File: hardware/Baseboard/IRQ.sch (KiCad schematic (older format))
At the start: 4 parts, among them IC11 74HC148, IC12 74HC273

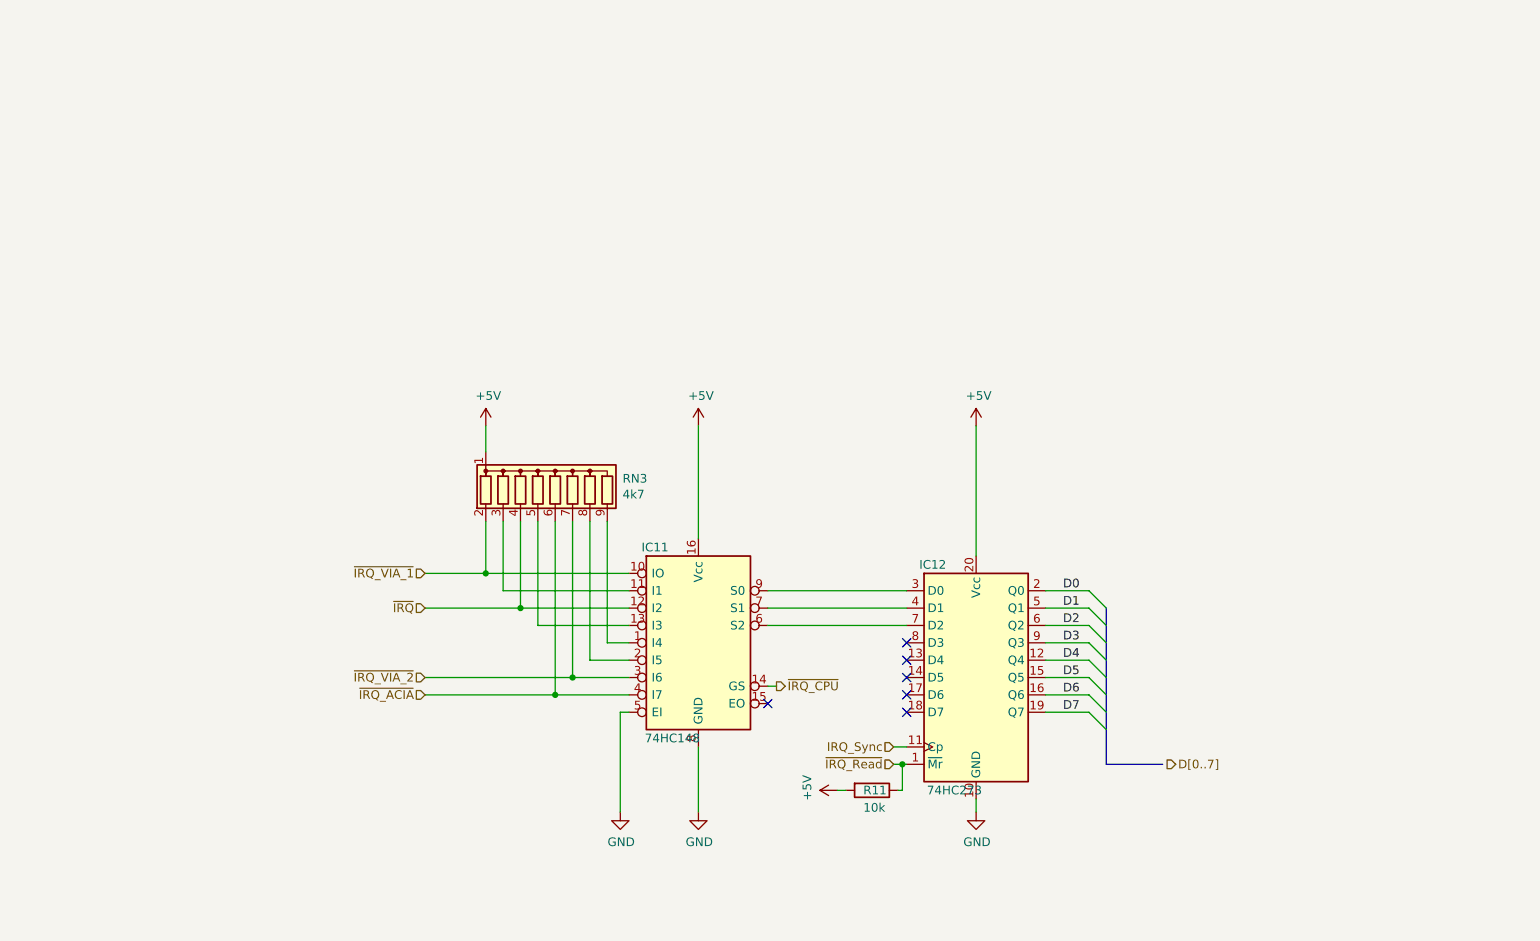
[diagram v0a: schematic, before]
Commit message: Improve routing, add some datasheet recommendations
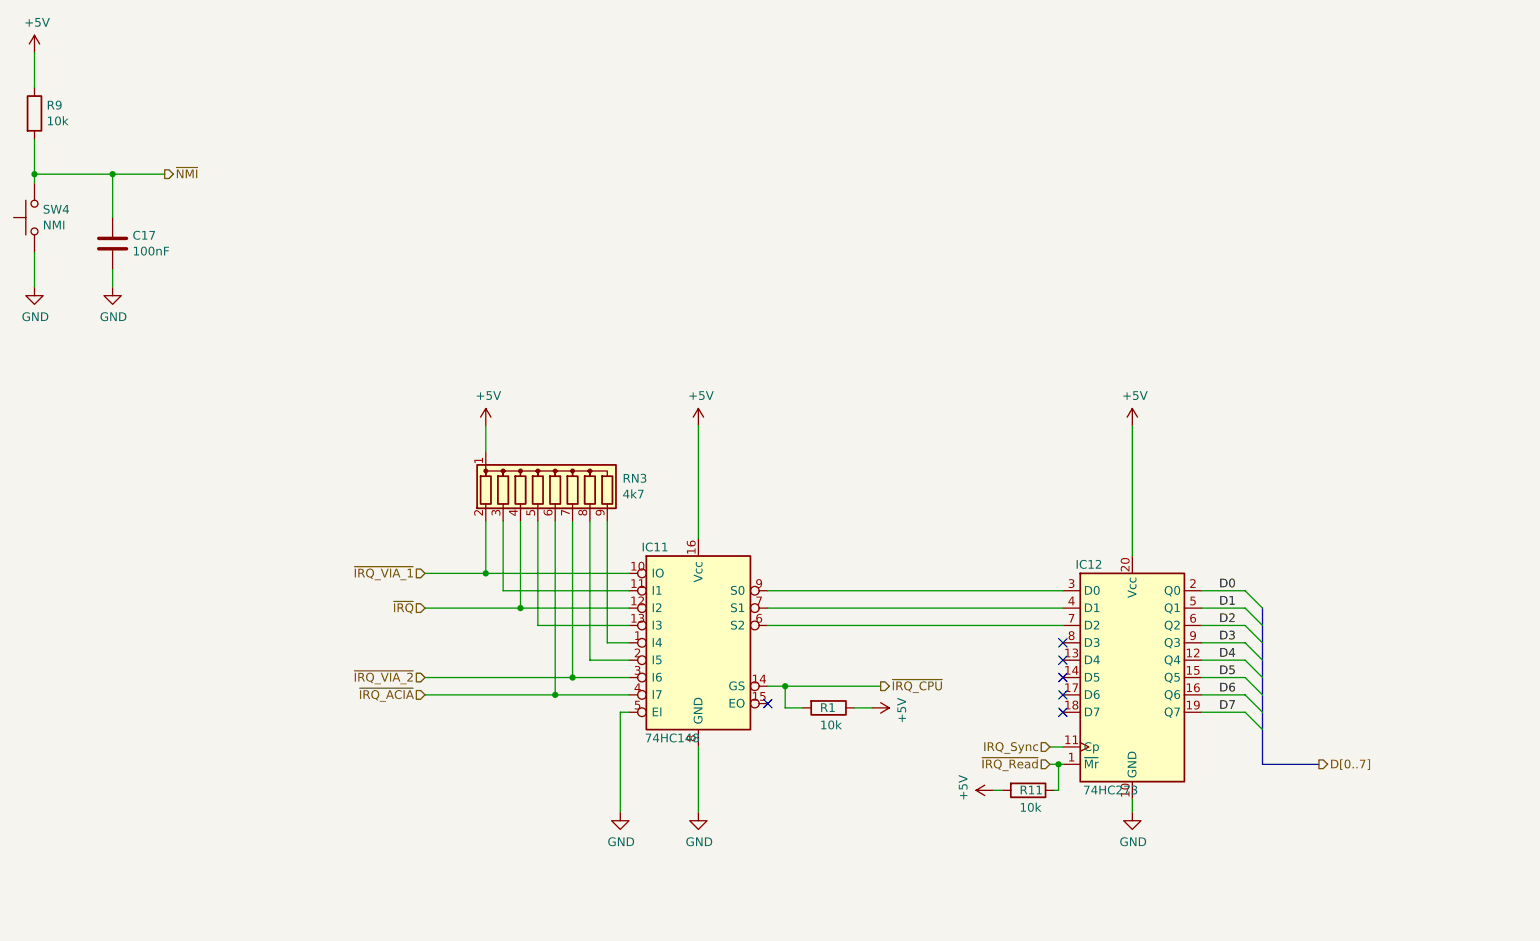
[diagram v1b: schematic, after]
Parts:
- added C17: 100nF, Capacitor_THT:C_Rect_L4.0mm_W2.5mm_P2.50mm, symbol Device:C
- added R1, R9: 10k, Resistor_THT:R_Axial_DIN0207_L6.3mm_D2.5mm_P7.62mm_Horizontal, symbol Device:R
- added SW4: NMI, Button_Switch_THT:SW_PUSH_6mm_H4.3mm, symbol Switch:SW_Push
- IC11: footprint Package_DIP:DIP-16_W7.62mm -> Package_DIP:DIP-16_W7.62mm_LongPads
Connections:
- net +5V: now also R1.1, R9.1
- net GND: now also C17.2, SW4.1
- net ~IRQ_CPU: now also R1.2
- new net ~NMI: C17.1, R9.2, SW4.2
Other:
- moved on the sheet: IC12, R11

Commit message: Optimize routing
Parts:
- IC12: footprint Package_DIP:DIP-20_W7.62mm -> Package_DIP:DIP-20_W7.62mm_LongPads
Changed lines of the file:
@@
 F 0 "IC12" H 6950 5175 50  0000 C CNN
 F 1 "74HC273" H 7075 3875 50  0000 C CNN
-F 2 "Package_DIP:DIP-20_W7.62mm" H 7200 4525 50  0001 C CNN
+F 2 "Package_DIP:DIP-20_W7.62mm_LongPads" H 7200 4525 50  0001 C CNN
 F 3 "https://assets.nexperia.com/documents/data-sheet/74HC_HCT273.pdf" H 7200 4525 50  0001 C CNN
 F 4 "Texas Instruments" H 7200 4525 50  0001 C CNN "Mfr."

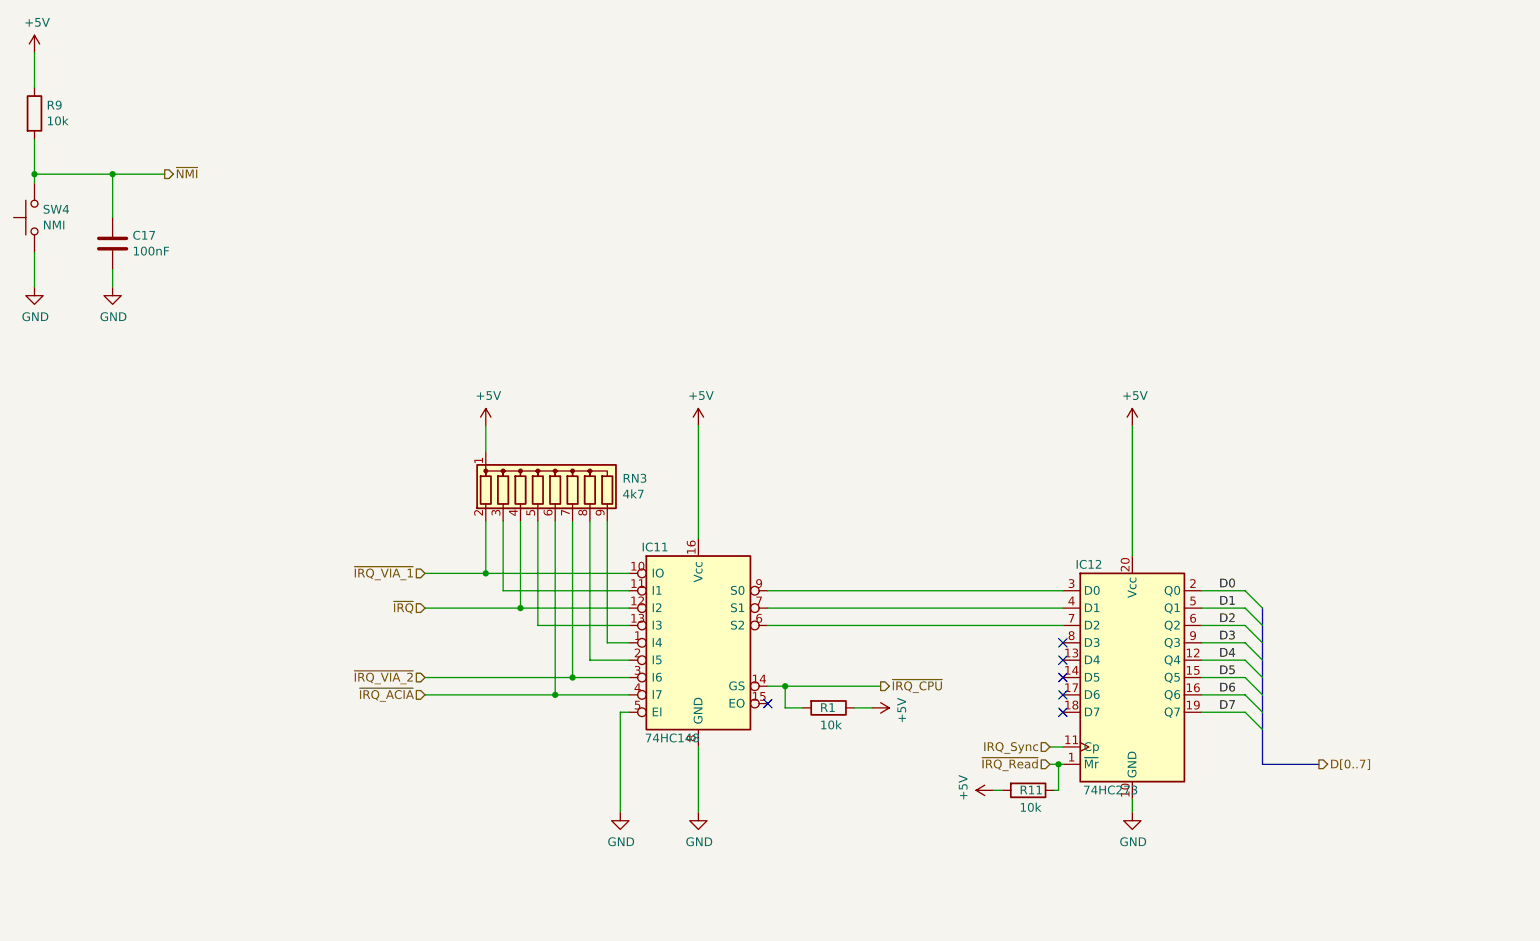
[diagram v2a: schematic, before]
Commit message: Optimize routing, add RDY and SYNC to expansion header
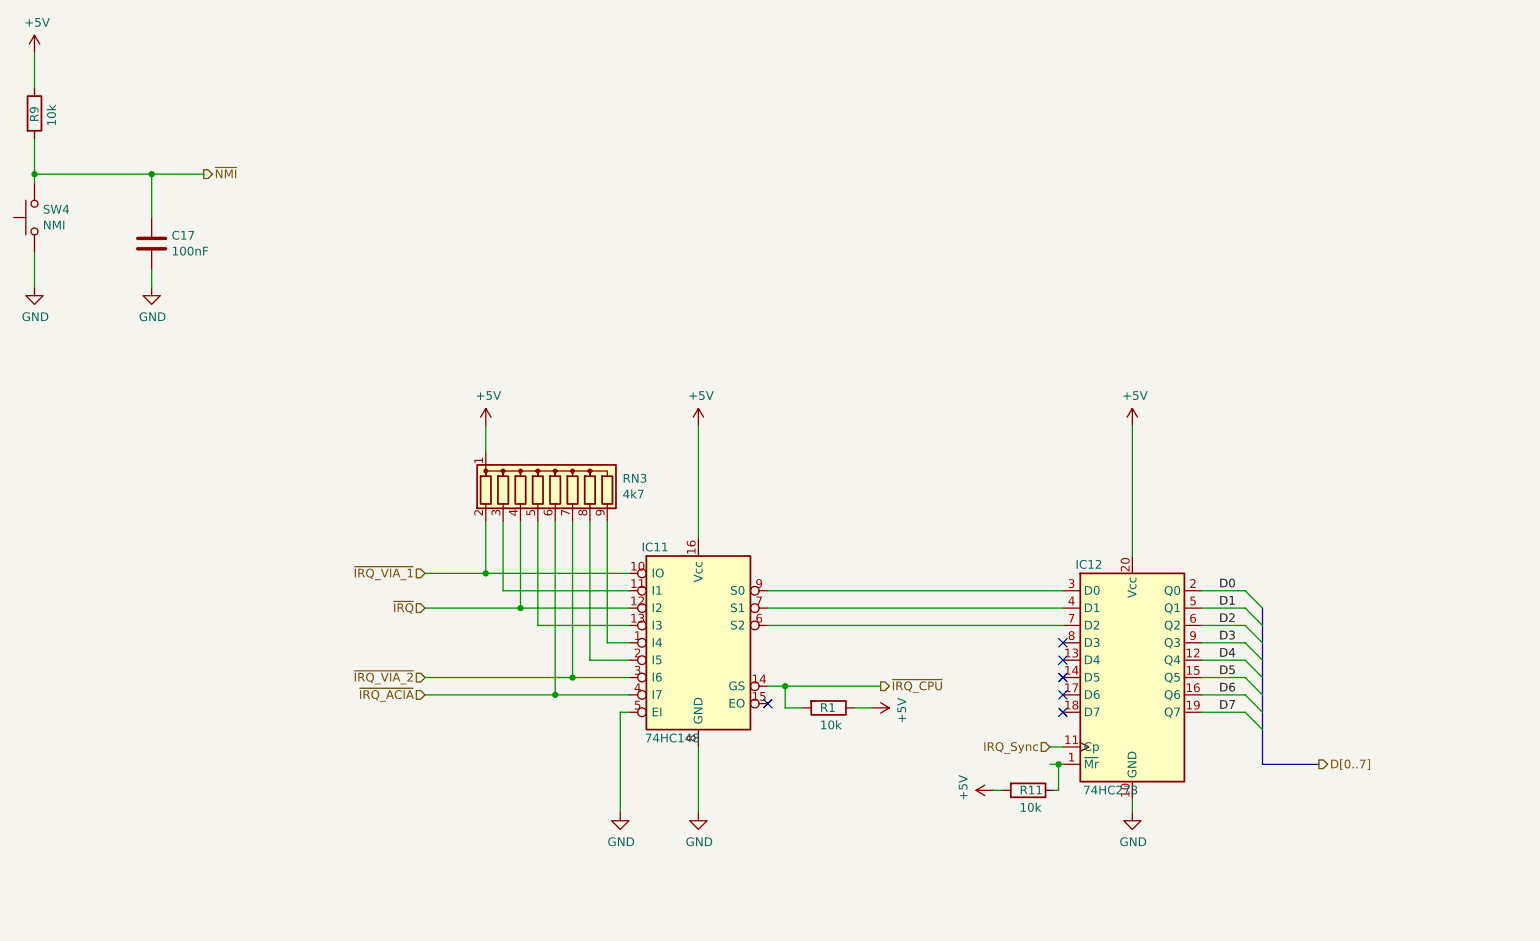
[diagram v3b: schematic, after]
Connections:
- net ~IRQ_Read: no longer names the net of IC12.1 (~Mr), R11.1
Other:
- moved on the sheet: C17
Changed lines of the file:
@@
 NoConn ~ 6800 4625
 NoConn ~ 6800 4725
-Text HLabel 6725 5025 0    50   Input ~ 0
-~IRQ_Read
 Wire Wire Line
 	6725 5025 6775 5025
@@
 AR Path="/5EC67F7B/5DE0C707" Ref="R?"  Part="1"
 AR Path="/5E710B5B/5DE0C707" Ref="R9"  Part="1"
-F 0 "R9" H 945 1321 50  0000 L CNN
-F 1 "10k" H 945 1230 50  0000 L CNN
+F 0 "R9" V 875 1225 50  0000 L CNN
+F 1 "10k" V 975 1200 50  0000 L CNN
 F 2 "Resistor_THT:R_Axial_DIN0207_L6.3mm_D2.5mm_P7.62mm_Horizontal" V 805 1275 50  0001 C CNN
 F 3 "https://www.mouser.de/datasheet/2/447/Yageo%20LR_MFP_2013-594635.pdf" H 875 1275 50  0001 C CNN
@@
 L Device:C C?
 U 1 1 5DE0C726
-P 1325 2025
+P 1550 2025
 AR Path="/5DE0C726" Ref="C?"  Part="1"
 AR Path="/5E9728CC/5DE0C726" Ref="C?"  Part="1"
 AR Path="/5EC67F7B/5DE0C726" Ref="C?"  Part="1"
 AR Path="/5E710B5B/5DE0C726" Ref="C17"  Part="1"
-F 0 "C17" H 1440 2071 50  0000 L CNN
-F 1 "100nF" H 1440 1980 50  0000 L CNN
-F 2 "Capacitor_THT:C_Rect_L4.0mm_W2.5mm_P2.50mm" H 1363 1875 50  0001 C CNN
-F 3 "https://www.mouser.de/datasheet/2/400/eadmlcc_halogenfree_fa150_en-890480.pdf" H 1325 2025 50  0001 C CNN
-F 4 "TDK" H 1325 2025 50  0001 C CNN "Mfr."
-F 5 "FA18X8R1H104KRU06" H 1325 2025 50  0001 C CNN "Mfr. No."
-F 6 "810-FA18X8R1H104KRU6" H 1325 2025 50  0001 C CNN "Mouser"
-	1    1325 2025
+F 0 "C17" H 1665 2071 50  0000 L CNN
+F 1 "100nF" H 1665 1980 50  0000 L CNN
+F 2 "Capacitor_THT:C_Rect_L4.0mm_W2.5mm_P2.50mm" H 1588 1875 50  0001 C CNN
+F 3 "https://www.mouser.de/datasheet/2/400/eadmlcc_halogenfree_fa150_en-890480.pdf" H 1550 2025 50  0001 C CNN
+F 4 "TDK" H 1550 2025 50  0001 C CNN "Mfr."
+F 5 "FA18X8R1H104KRU06" H 1550 2025 50  0001 C CNN "Mfr. No."
+F 6 "810-FA18X8R1H104KRU6" H 1550 2025 50  0001 C CNN "Mouser"
+	1    1550 2025
 	1    0    0    -1
 $EndComp
@@
 	875  1425 875  1625
 Wire Wire Line
-	875  1625 1325 1625
-Wire Wire Line
-	1325 1625 1325 1875
+	1550 1625 1550 1875
 Connection ~ 875  1625
 Wire Wire Line
@@
 L power:GND #PWR?
 U 1 1 5DE0C731
-P 1325 2275
+P 1550 2275
 AR Path="/5DE0C731" Ref="#PWR?"  Part="1"
 AR Path="/5E9728CC/5DE0C731" Ref="#PWR?"  Part="1"
 AR Path="/5EC67F7B/5DE0C731" Ref="#PWR?"  Part="1"
 AR Path="/5E710B5B/5DE0C731" Ref="#PWR0106"  Part="1"
-F 0 "#PWR0106" H 1325 2025 50  0001 C CNN
-F 1 "GND" H 1330 2102 50  0000 C CNN
-F 2 "" H 1325 2275 50  0001 C CNN
-F 3 "" H 1325 2275 50  0001 C CNN
-	1    1325 2275
-	1    0    0    -1
-$EndComp
-Connection ~ 1325 1625
+F 0 "#PWR0106" H 1550 2025 50  0001 C CNN
+F 1 "GND" H 1555 2102 50  0000 C CNN
+F 2 "" H 1550 2275 50  0001 C CNN
+F 3 "" H 1550 2275 50  0001 C CNN
+	1    1550 2275
+	1    0    0    -1
+$EndComp
+Connection ~ 1550 1625
 Wire Wire Line
 	875  2075 875  2275
 Wire Wire Line
-	1325 2175 1325 2275
-Wire Wire Line
-	1325 1625 1625 1625
-Text HLabel 1625 1625 2    50   Output ~ 0
+	1550 2175 1550 2275
+Wire Wire Line
+	1550 1625 1850 1625
+Text HLabel 1850 1625 2    50   Output ~ 0
 ~NMI
 Wire Wire Line
@@
 Wire Wire Line
 	5200 4575 5750 4575
+Wire Wire Line
+	875  1625 1550 1625
 Wire Bus Line
 	7950 4125 7950 5025

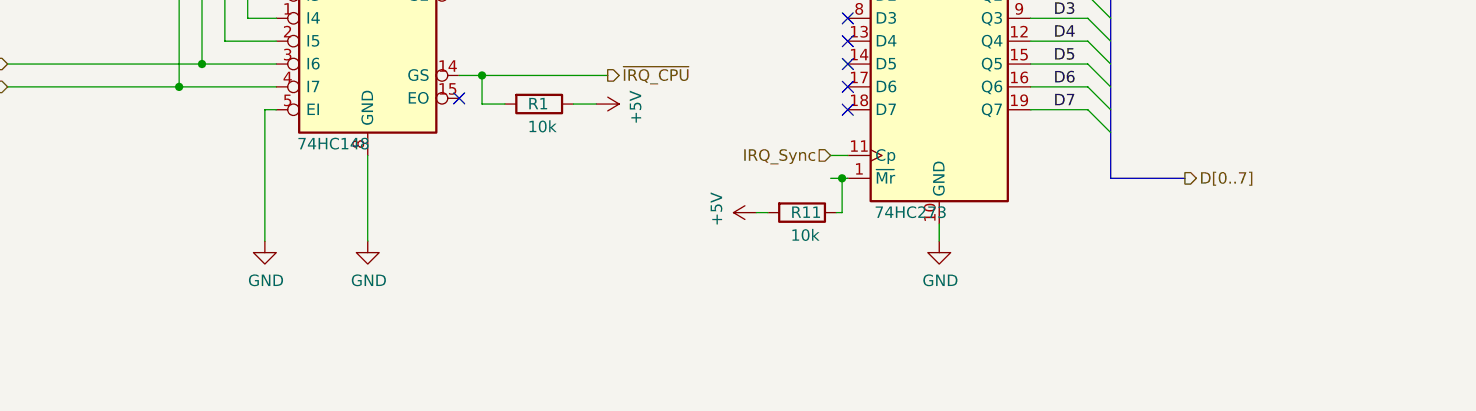
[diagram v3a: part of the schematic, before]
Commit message: Add note to IRQ schematic
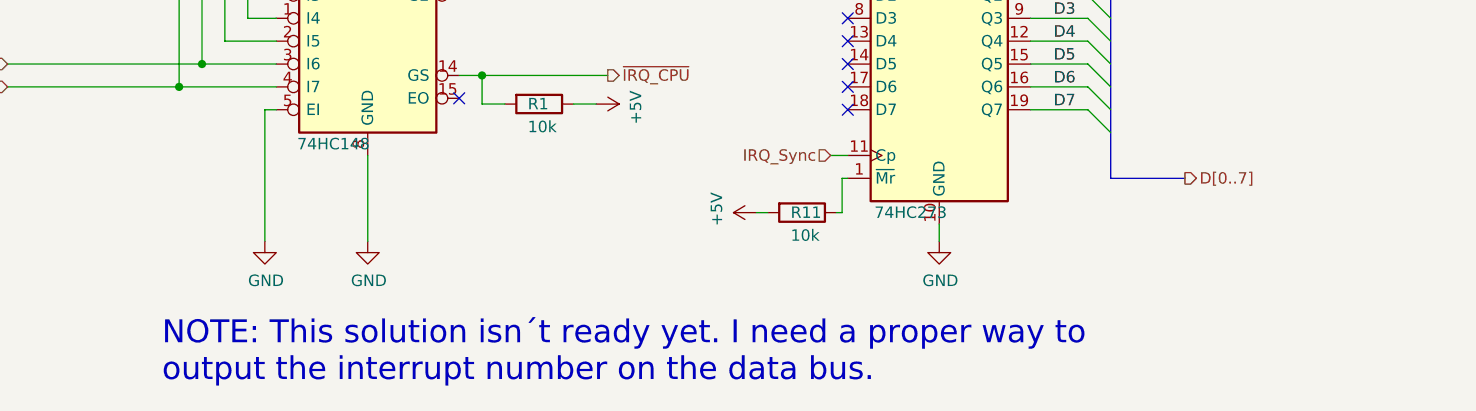
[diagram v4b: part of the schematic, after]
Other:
- note added: "NOTE: This solution isn´t ready yet. I need a proper way to\noutput the interrupt number on the data bus."
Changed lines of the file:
@@
 NoConn ~ 6800 4625
 NoConn ~ 6800 4725
-Wire Wire Line
-	6725 5025 6775 5025
 NoConn ~ 5100 4675
 $Comp
@@
 Wire Wire Line
 	6775 5025 6775 5175
-Connection ~ 6775 5025
 Wire Wire Line
 	6775 5025 6800 5025
@@
 Wire Bus Line
 	7950 4125 7950 5025
+Text Notes 3800 5925 0    100  ~ 0
+NOTE: This solution isn´t ready yet. I need a proper way to\noutput the interrupt number on the data bus.
 $EndSCHEMATC
